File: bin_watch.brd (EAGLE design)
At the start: 42.9 x 35.4 mm, 89 parts, among them IC1 MEGA48/88/168-AU, J1 USB3100-XX-X_REVB, P1 50k, Q1 32.768kHz, T1 2N7002BKV, T2 2N7002BKV, T3 2N7002BKV, T4 2N7002BKV, T5 PMDT670UPE, T6 PMDT670UPE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

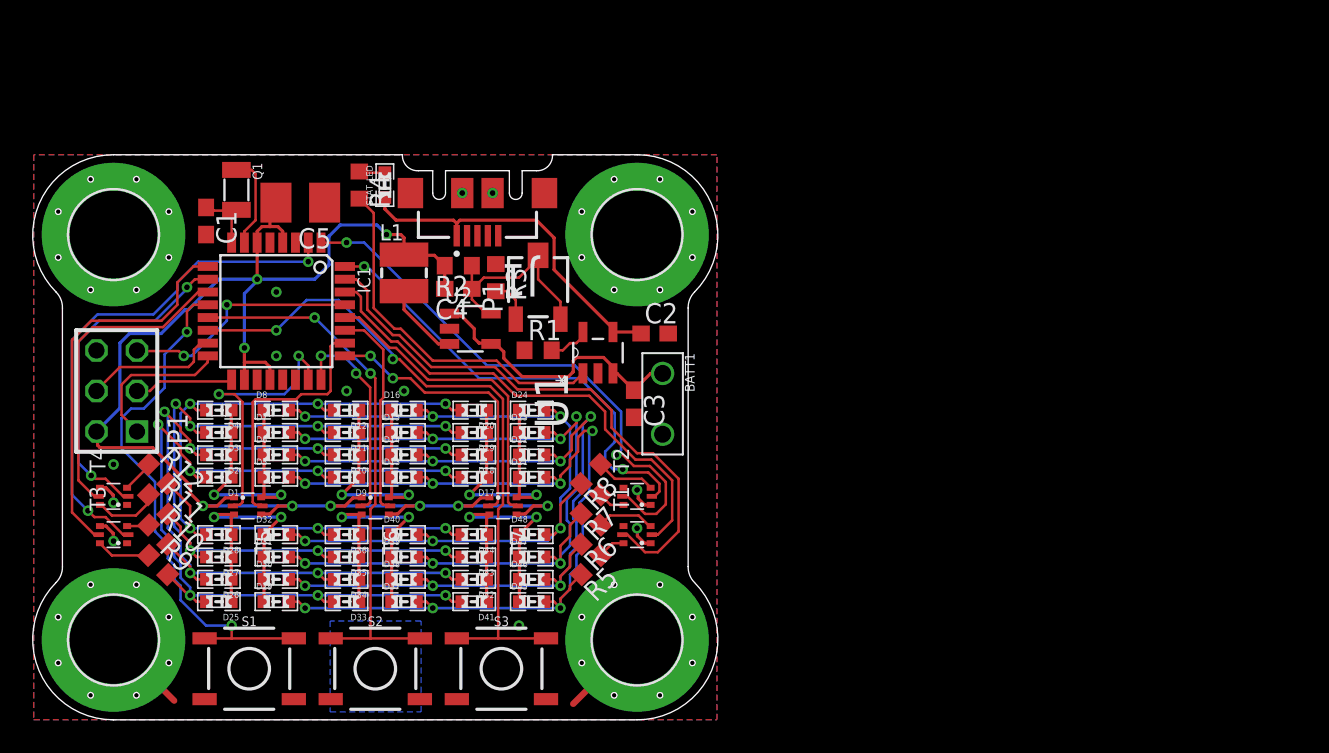
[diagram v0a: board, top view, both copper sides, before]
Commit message: Added fiducial marks
Some minor adjustments to the traces, and added fiducial marks for the board and for the chip.
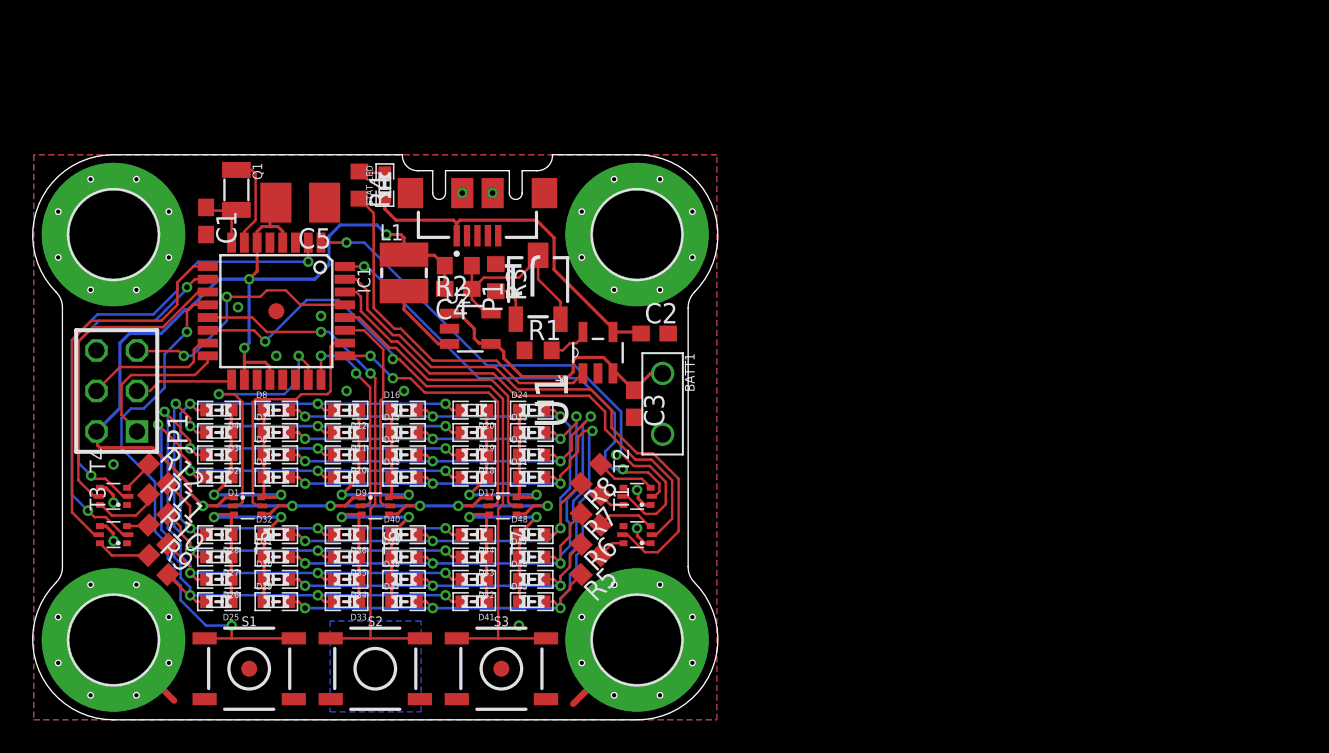
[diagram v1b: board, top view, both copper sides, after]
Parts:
- added U$1, U$2, U$3: FIDUCIAL, adafruit:FIDUCIAL_1MM
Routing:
- net RST: track 15.1 -> 16.1 mm
- net MOSI: track 9.29 -> 8.67 mm
- net PB2: track 42.7 -> 43.3 mm
- net GND: vias 12 -> 13

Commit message: Fixed silkscreen width issue
MetaLab logo now renders correctly at 500 DPI
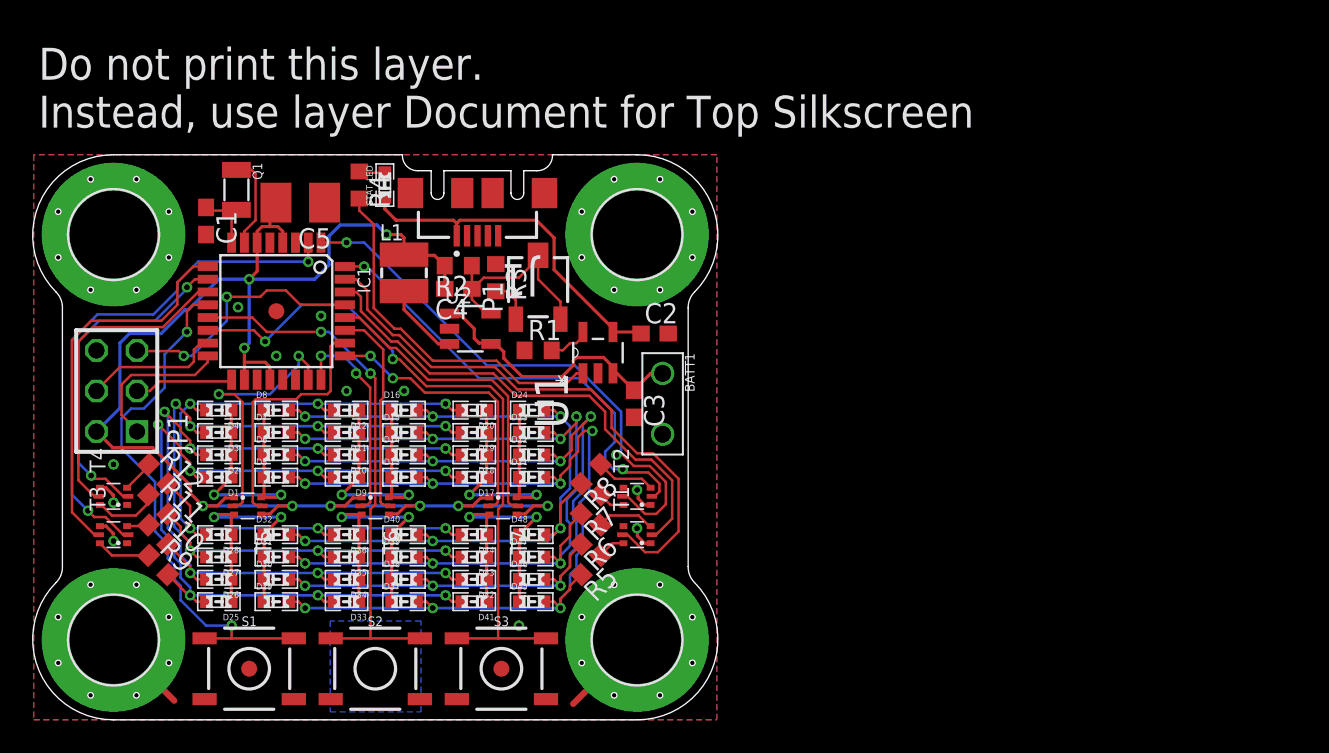
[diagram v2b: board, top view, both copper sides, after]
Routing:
- net PC0: track 17.3 -> 16.7 mm
- net GND: vias 13 -> 11
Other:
- outline, holes or cut-outs redrawn
- board text added: "Do not print this layer. Instead, use layer Document for Top Silkscreen"
- board text added: "github/programagor/uChronos"
- board text removed: "2017"
- board text removed: "OSHW"

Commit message: Changed power supply to 5V
Replaced the Buck converter with a Boost converter. Saved some space.
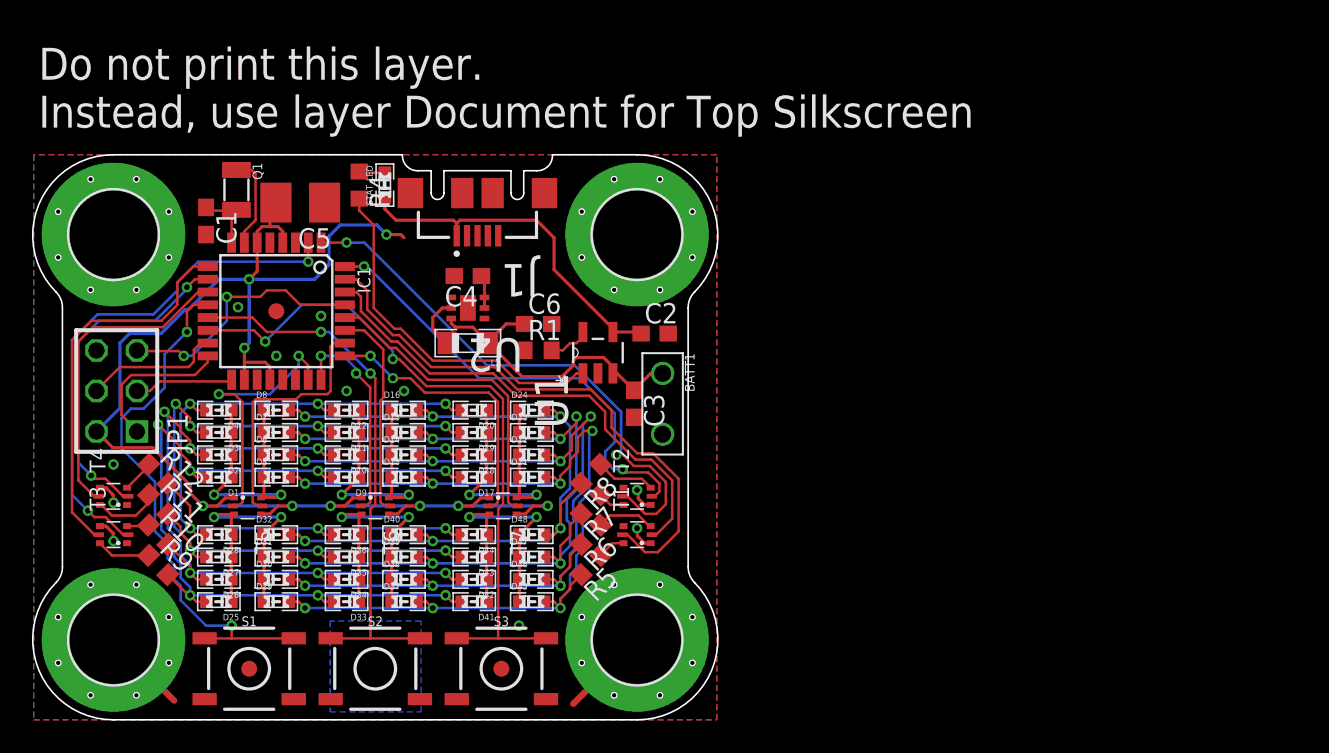
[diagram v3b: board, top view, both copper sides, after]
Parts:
- removed P1: 50k, pot:3223J
- removed R2: 1M3, rcl:R0603
- removed R3: 255k, rcl:R0603
- added C6: 4.7u, rcl:C0603
- C4: value 3p -> 4.7u
- L1: value 2.2u -> (none); device inductor:CC-ME3220 -> standardparts:0805
- U2: value RT8059 -> TPS61240DRVT; device pmg-library:TSOT23-5 -> Texas Instruments_By_element14_Batch_1:SON65P200X200X80-7N
- moved L1 5.95 mm to (27.2, 23.6), turned to 180 degrees
- moved U2 1.31 mm to (27.2, 25.8), turned to 180 degrees
- moved C4 1.00 mm to (27.2, 27.8)
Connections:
- removed net FB: C4.1, P1.2, P1.3, R2.1, U2.6
- removed net LX: L1.P$1, U2.3
- removed net N$10: P1.1, R3.2
- new net L: L1.2, U2.5
- net GND: now also C4.2, C6.2, U2.1, U2.7; no longer R3.1, U2.2
- net VBATT: now also C6.1, L1.1, U2.6; no longer U2.1
- net VCC: now also C4.1, U2.2, U2.3; no longer C4.2, L1.P$2, R2.2
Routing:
- net FB: track 13.2 -> 0.00 mm
- net LX: track 4.90 -> 0.00 mm
- net L: track 0.00 -> 3.38 mm
- net VCC: track 93.6 -> 90.4 mm
- net N$10: track 2.68 -> 0.00 mm
- net VBATT: track 17.8 -> 19.9 mm

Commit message: Removed mounting holes
Saved a lot more space
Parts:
- removed H1, H3, H4, H6: MOUNT-PAD-ROUND5.5, holes:5,5-PAD
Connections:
- net GND: no longer H1.B5,5, H3.B5,5, H4.B5,5, H6.B5,5
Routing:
- net GND: track 17.1 -> 6.04 mm
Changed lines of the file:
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@@
 <layer number="42" name="bRestrict" color="1" fill="10" visible="no" active="yes"/>
 <layer number="43" name="vRestrict" color="2" fill="10" visible="no" active="yes"/>
-<layer number="44" name="Drills" color="7" fill="1" visible="no" active="yes"/>
-<layer number="45" name="Holes" color="7" fill="1" visible="no" active="yes"/>
+<layer number="44" name="Drills" color="7" fill="1" visible="yes" active="yes"/>
+<layer number="45" name="Holes" color="7" fill="1" visible="yes" active="yes"/>
 <layer number="46" name="Milling" color="3" fill="1" visible="no" active="yes"/>
 <layer number="47" name="Measures" color="7" fill="1" visible="no" active="yes"/>
@@
 <rectangle x1="19.8095" y1="0.74285625" x2="20.05711875" y2="1.98095" layer="42"/>
 <rectangle x1="20.05711875" y1="0.990475" x2="20.3047375" y2="1.4857125" layer="42"/>
-<hole x="8.464546875" y="6.4350625" drill="0.35"/>
-<hole x="6.4350625" y="8.464546875" drill="0.35"/>
-<hole x="3.5649375" y="8.464546875" drill="0.35"/>
-<hole x="1.535453125" y="6.4350625" drill="0.35"/>
-<hole x="1.535453125" y="3.5649375" drill="0.35"/>
-<hole x="3.5649375" y="1.535453125" drill="0.35"/>
-<hole x="6.4350625" y="1.535453125" drill="0.35"/>
-<hole x="8.464546875" y="3.5649375" drill="0.35"/>
-<hole x="41.264546875" y="6.4350625" drill="0.35"/>
-<hole x="39.2350625" y="8.464546875" drill="0.35"/>
-<hole x="36.3649375" y="8.464546875" drill="0.35"/>
-<hole x="34.335453125" y="6.4350625" drill="0.35"/>
-<hole x="34.335453125" y="3.5649375" drill="0.35"/>
-<hole x="36.3649375" y="1.535453125" drill="0.35"/>
-<hole x="39.2350625" y="1.535453125" drill="0.35"/>
-<hole x="41.264546875" y="3.5649375" drill="0.35"/>
-<hole x="41.264546875" y="31.8350625" drill="0.35"/>
-<hole x="39.2350625" y="33.864546875" drill="0.35"/>
-<hole x="36.3649375" y="33.864546875" drill="0.35"/>
-<hole x="34.335453125" y="31.8350625" drill="0.35"/>
-<hole x="34.335453125" y="28.9649375" drill="0.35"/>
-<hole x="36.3649375" y="26.935453125" drill="0.35"/>
-<hole x="39.2350625" y="26.935453125" drill="0.35"/>
-<hole x="41.264546875" y="28.9649375" drill="0.35"/>
-<hole x="8.464546875" y="31.8350625" drill="0.35"/>
-<hole x="6.4350625" y="33.864546875" drill="0.35"/>
-<hole x="3.5649375" y="33.864546875" drill="0.35"/>
-<hole x="1.535453125" y="31.8350625" drill="0.35"/>
-<hole x="1.535453125" y="28.9649375" drill="0.35"/>
-<hole x="3.5649375" y="26.935453125" drill="0.35"/>
-<hole x="6.4350625" y="26.935453125" drill="0.35"/>
-<hole x="8.464546875" y="28.9649375" drill="0.35"/>
 <wire x1="12.43" y1="18.59" x2="12.43" y2="18.238" width="0.06" layer="22"/>
 <wire x1="12.43" y1="18.238" x2="12.43" y2="17.743" width="0.06" layer="22"/>
@@
 <attribute name="SF_SKU" value="COM-08720" x="29.3" y="3.2" size="1.778" layer="27" display="off"/>
 </element>
-<element name="H1" library="holes" library_urn="urn:adsk.eagle:library:237" package="5,5-PAD" value="MOUNT-PAD-ROUND5.5" x="5" y="30.4"/>
-<element name="H3" library="holes" library_urn="urn:adsk.eagle:library:237" package="5,5-PAD" value="MOUNT-PAD-ROUND5.5" x="37.8" y="30.4"/>
-<element name="H4" library="holes" library_urn="urn:adsk.eagle:library:237" package="5,5-PAD" value="MOUNT-PAD-ROUND5.5" x="5" y="5"/>
-<element name="H6" library="holes" library_urn="urn:adsk.eagle:library:237" package="5,5-PAD" value="MOUNT-PAD-ROUND5.5" x="37.8" y="5"/>
 <element name="T1" library="nxp_60" package="SOT666" value="2N7002BKV" x="37.8" y="11.6" rot="R90"/>
 <element name="T2" library="nxp_60" package="SOT666" value="2N7002BKV" x="37.8" y="14" rot="R90"/>
@@
 <contactref element="S3" pad="3"/>
 <contactref element="S3" pad="4"/>
-<contactref element="H1" pad="B5,5"/>
-<contactref element="H3" pad="B5,5"/>
-<contactref element="H4" pad="B5,5"/>
-<contactref element="H6" pad="B5,5"/>
 <contactref element="T1" pad="1"/>
 <contactref element="T1" pad="4"/>
@@
 <wire x1="4.981296875" y1="11.681296875" x2="4.981296875" y2="11.218703125" width="0.2" layer="1"/>
 <wire x1="4.981296875" y1="11.218703125" x2="5" y2="11.2" width="0.2" layer="1"/>
-<wire x1="8.8" y1="1.2" x2="5" y2="5" width="0.4" layer="1"/>
-<wire x1="33.8" y1="1" x2="37.8" y2="5" width="0.4" layer="1"/>
 <via x="15.2" y="22.8" extent="1-16" drill="0.35"/>
 <contactref element="U1" pad="2"/>
@@
 <contactref element="U2" pad="7"/>
 <contactref element="C6" pad="2"/>
+<wire x1="32.094" y1="1.295" x2="30.4" y2="5.9" width="0" layer="19" extent="1-1"/>
+<wire x1="36.95" y1="12.138" x2="30.4" y2="5.9" width="0" layer="19" extent="1-1"/>
+<wire x1="5" y1="16" x2="3.93" y2="23.14" width="0" layer="19" extent="1-1"/>
 </signal>
 <signal name="XTAL_N">

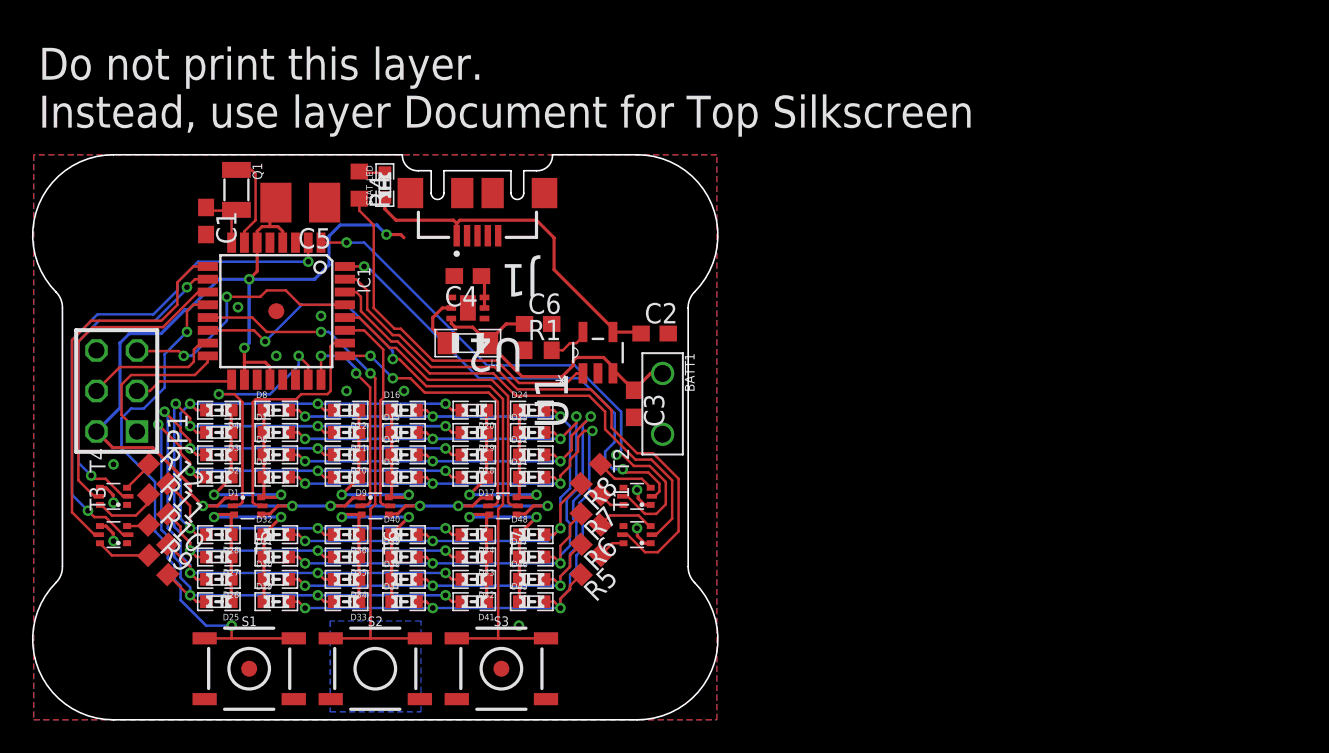
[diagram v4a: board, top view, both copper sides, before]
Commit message: Added charger isolation
When the battery is being charged, the Boost converter is powered directly from USB rather than through the charger.
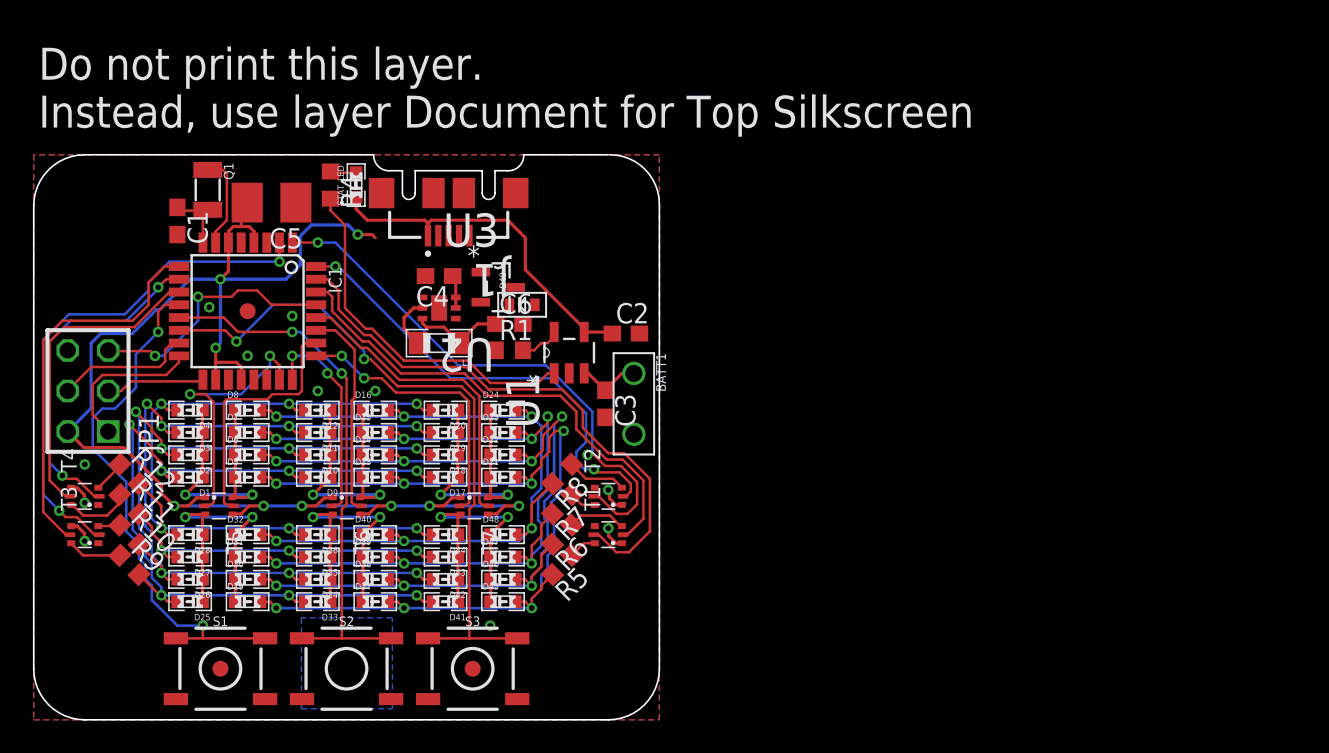
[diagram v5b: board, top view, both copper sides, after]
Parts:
- added D49: (no value), adafruit:SOD-523
- added U3: PMV65XP, NXP_By_element14_Batch_1:SOT95P230X110-3N
- R10, R11, R12, R5, R6, R7, R8, R9: value 12 -> 68
- moved C3 1.80 mm to (35.8, 19.8)
- moved U1 1.80 mm to (33.5, 23.0)
- moved C1 1.80 mm to (9.00, 31.2)
- moved C4 1.80 mm to (25.4, 27.8)
- moved C6 1.80 mm to (29.8, 24.8)
- moved D10 1.80 mm to (17.8, 16.6)
- moved D11 1.80 mm to (17.8, 18.0)
- moved D12 1.80 mm to (17.8, 19.4)
- moved D13 1.80 mm to (21.4, 15.2)
- moved D14 1.80 mm to (21.4, 16.6)
- moved D15 1.80 mm to (21.4, 18.0)
- moved D16 1.80 mm to (21.4, 19.4)
- moved D17 1.80 mm to (25.8, 15.2)
- moved D18 1.80 mm to (25.8, 16.6)
- moved D19 1.80 mm to (25.8, 18.0)
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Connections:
- new net VIN: C6.1, D49.K, L1.1, U2.4, U2.6, U3.2
- net VBATT: now also U3.3; no longer C6.1, L1.1, U2.4, U2.6
- net VBUS: now also D49.A, U3.1
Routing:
- net VBATT: track 19.9 -> 3.98 mm
- net VIN: track 0.00 -> 5.96 mm
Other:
- board size 42.9 x 35.4 mm -> 39.2 x 35.4 mm

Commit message: 4-layer design
Now using ground and power plane
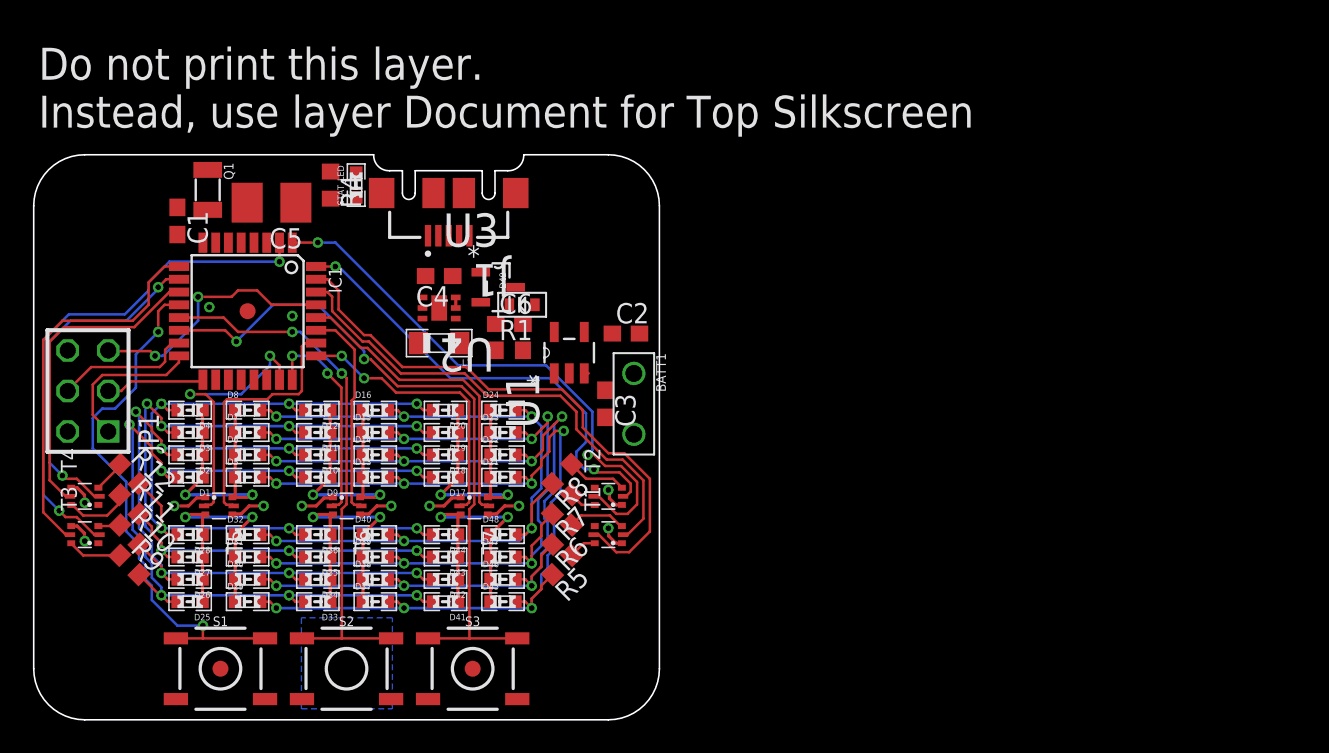
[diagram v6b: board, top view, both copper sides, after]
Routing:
- net VCC: track 90.4 -> 14.1 mm, vias 9 -> 6
- net STAT: track 22.5 -> 0.00 mm
- net VBUS: track 22.2 -> 0.13 mm
- net VIN: track 5.96 -> 0.00 mm
- net XTAL_P: track 5.90 -> 0.00 mm
- net XTAL_N: track 4.11 -> 0.00 mm
- net VBATT: track 3.98 -> 0.26 mm
- net L: track 3.38 -> 0.00 mm
- net PROG: track 2.60 -> 0.00 mm
- net N$3: track 1.63 -> 0.00 mm
- net GND: vias 11 -> 6
- added copper zone on layer 2, net GND
- added copper zone on layer 15, net VCC
- removed copper zone on layer 1, net GND
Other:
- outline, holes or cut-outs redrawn
